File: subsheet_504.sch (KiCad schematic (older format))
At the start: 36 parts, among them J502 Phono LEFT, J503 Phono RIGHT, U504 LF347N_mu, U508 LMC1992CCN_PHY

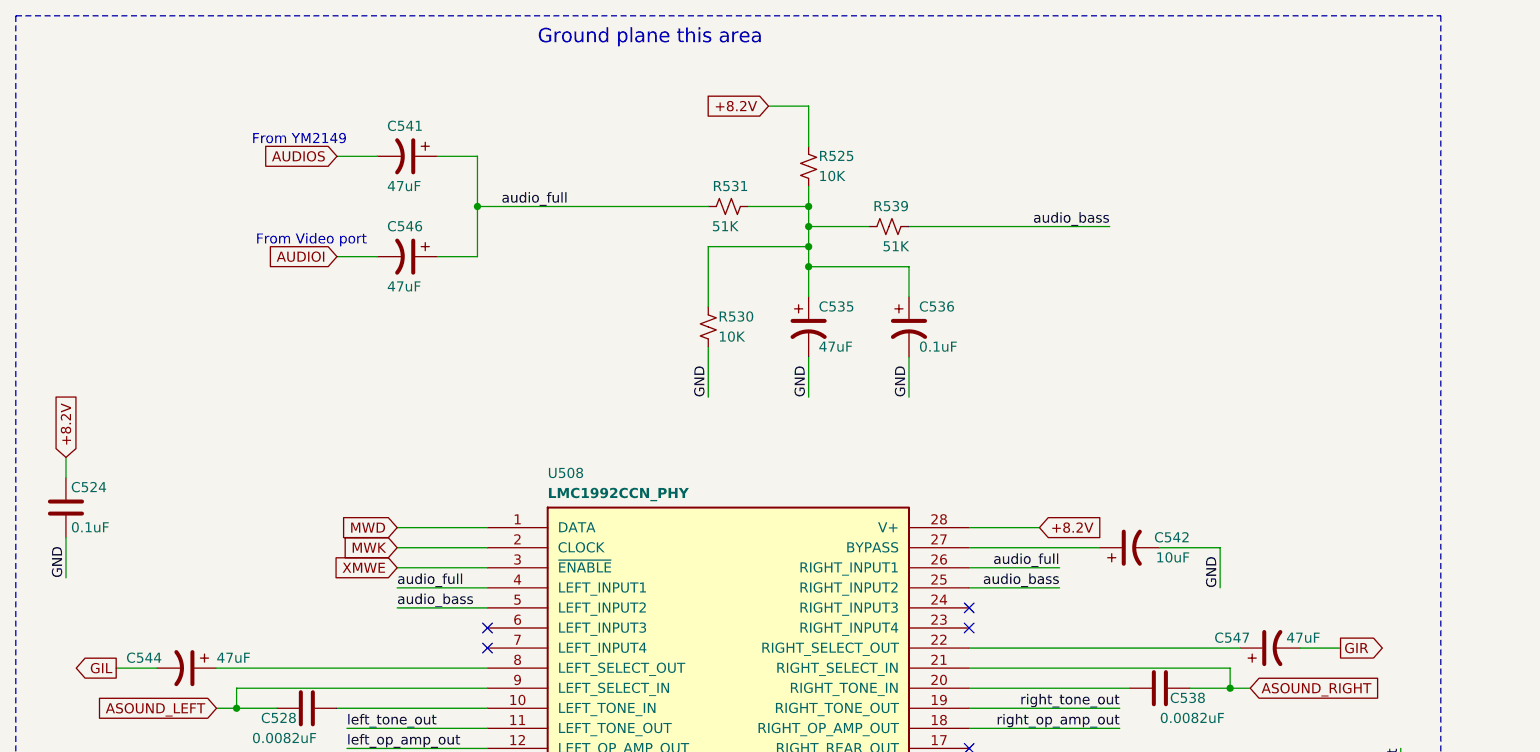
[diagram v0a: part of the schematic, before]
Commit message: [Schematic] mention and reference of the LMC Mixer fix
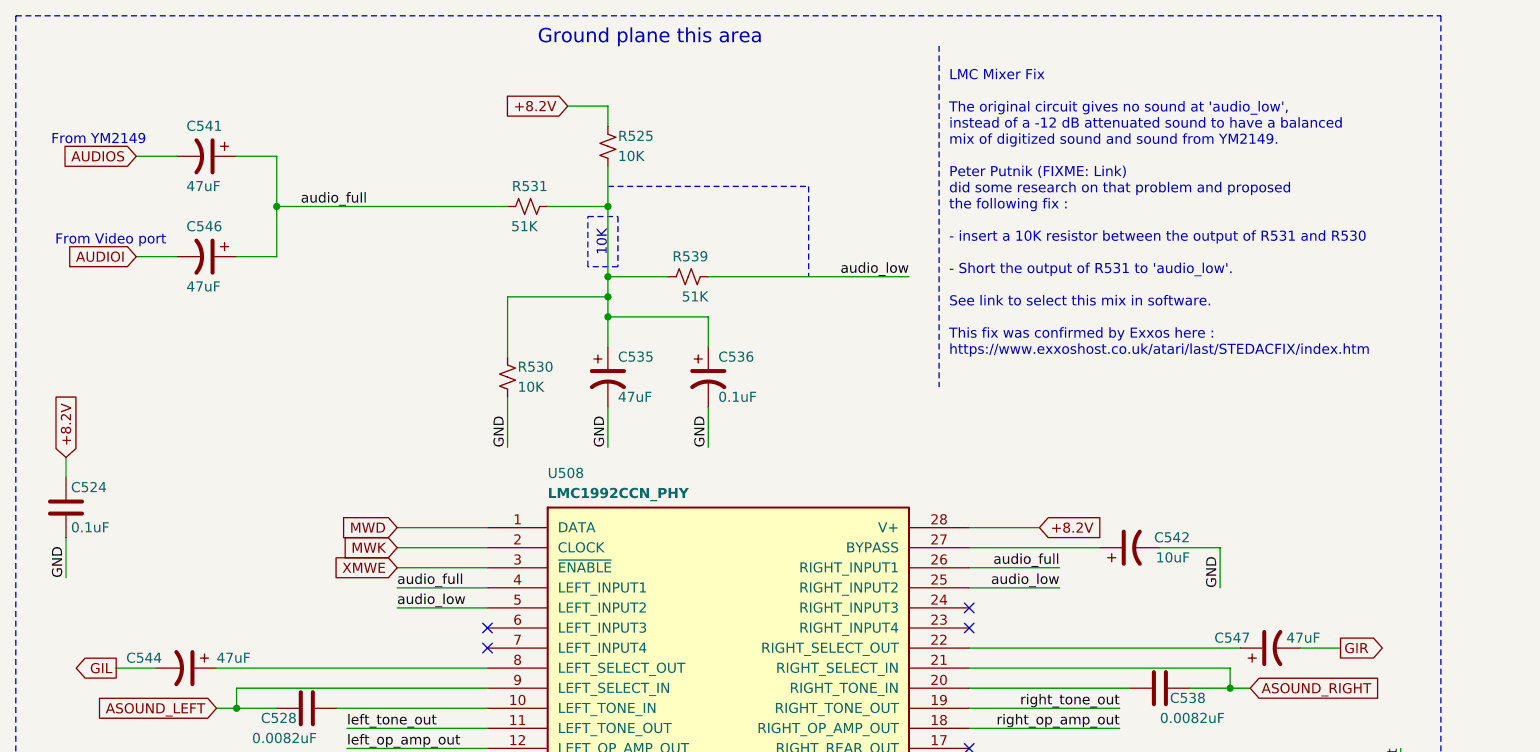
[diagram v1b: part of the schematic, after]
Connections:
- net audio_bass renamed audio_low
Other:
- note added: "10K"
- note added: "LMC Mixer Fix\n\nThe original circuit gives no sound at 'audio_low',\ninstead of a -12 dB attenuated sound to have a balanced\nmix of digitized sound and sound from YM2149.\n\nPeter Putnik (FIXME: Link) \ndid some research on that problem and proposed \nthe following fix :\n\n- insert a 10K resistor between the output of R531 and R530\n\n- Short the output of R531 to 'audio_low'. \n\nSee link to 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"
- moved on the sheet: C535, C536, C541, C546, R525, R530, R531, R539

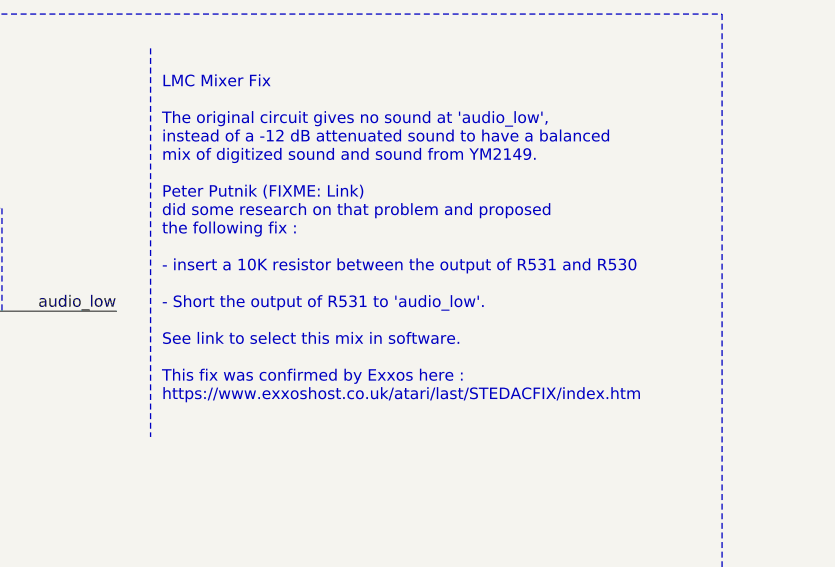
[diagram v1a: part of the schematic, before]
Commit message: [Schematics] finalize comment about audio mix fix with reference link to P.P. page
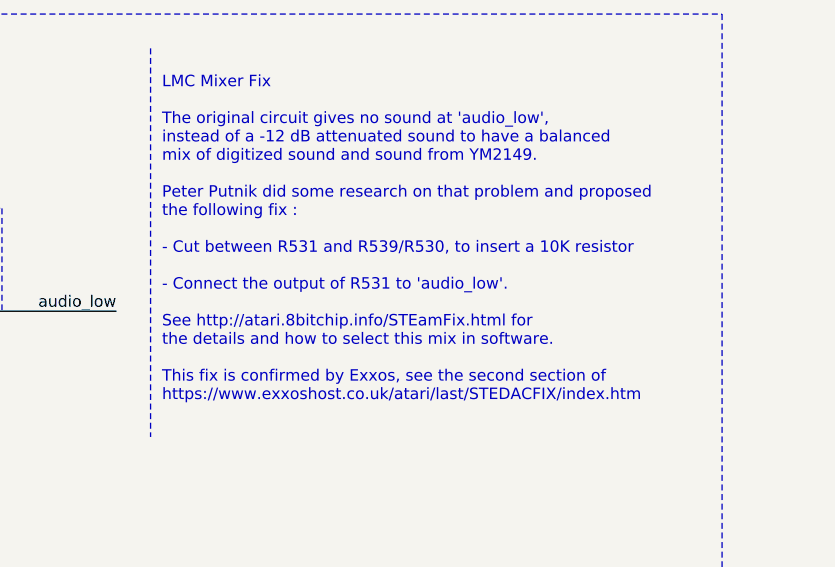
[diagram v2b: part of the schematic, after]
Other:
- note added: "LMC Mixer Fix\n\nThe original circuit gives no sound at 'audio_low',\ninstead of a -12 dB attenuated sound to have a balanced\nmix of digitized sound and sound from YM2149.\n\nPeter Putnik did some research on that problem and proposed \nthe following fix :\n\n- Cut between R531 and R539/R530, to insert a 10K resistor\n \n- Connect the output of R531 to 'audio_low'. \n\nSee http://atari.8bitchip.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"
- note removed: "LMC Mixer Fix\n\nThe original circuit gives no sound at 'audio_low',\ninstead of a -12 dB attenuated sound to have a balanced\nmix of digitized sound and sound from YM2149.\n\nPeter Putnik (FIXME: Link) \ndid some research on that problem and proposed \nthe following fix :\n\n- insert a 10K resistor between the output of R531 and R530\n\n- Short the output of R531 to 'audio_low'. \n\nSee link to 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"
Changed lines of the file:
@@
 	7450 4200 7450 4850
 Text Notes 5200 2250 0    50   ~ 0
-LMC Mixer Fix\n\nThe original circuit gives no sound at 'audio_low',\ninstead of a -12 dB attenuated sound to have a balanced\nmix of digitized sound and sound from YM2149.\n\nPeter Putnik (FIXME: Link) \ndid some research on that problem and proposed \nthe following fix :\n\n- insert a 10K resistor between the output of R531 and R530\n\n- Short the output of R531 to 'audio_low'. \n\nSee link to select this mix in software.\n\nThis fix was confirmed by Exxos here :\nhttps://www.exxoshost.co.uk/atari/last/STEDACFIX/index.htm
+LMC Mixer Fix\n\nThe original circuit gives no sound at 'audio_low',\ninstead of a -12 dB attenuated sound to have a balanced\nmix of digitized sound and sound from YM2149.\n\nPeter Putnik did some research on that problem and proposed \nthe following fix :\n\n- Cut between R531 and R539/R530, to insert a 10K resistor\n  \n- Connect the output of R531 to 'audio_low'. \n\nSee http://atari.8bitchip.info/STEamFix.html for \nthe details and how to select this mix in software.\n\nThis fix is confirmed by Exxos, see the second section of\nhttps://www.exxoshost.co.uk/atari/last/STEDACFIX/index.htm\n
 Connection ~ 3500 1950
 Text Notes 3500 1750 1    50   ~ 0

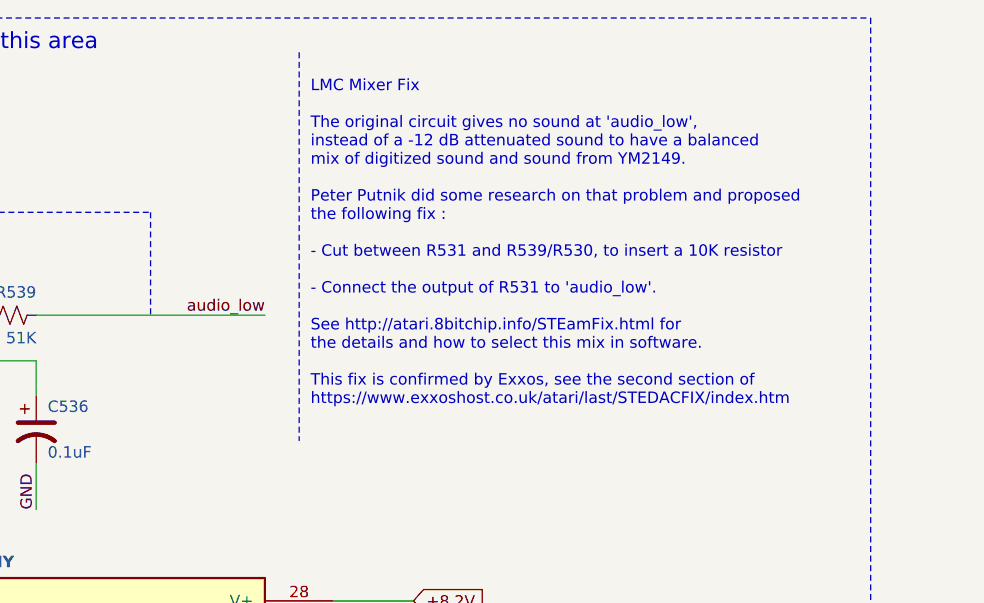
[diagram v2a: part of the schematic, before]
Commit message: Added a note about the presence of comment referencing some hardware fixes
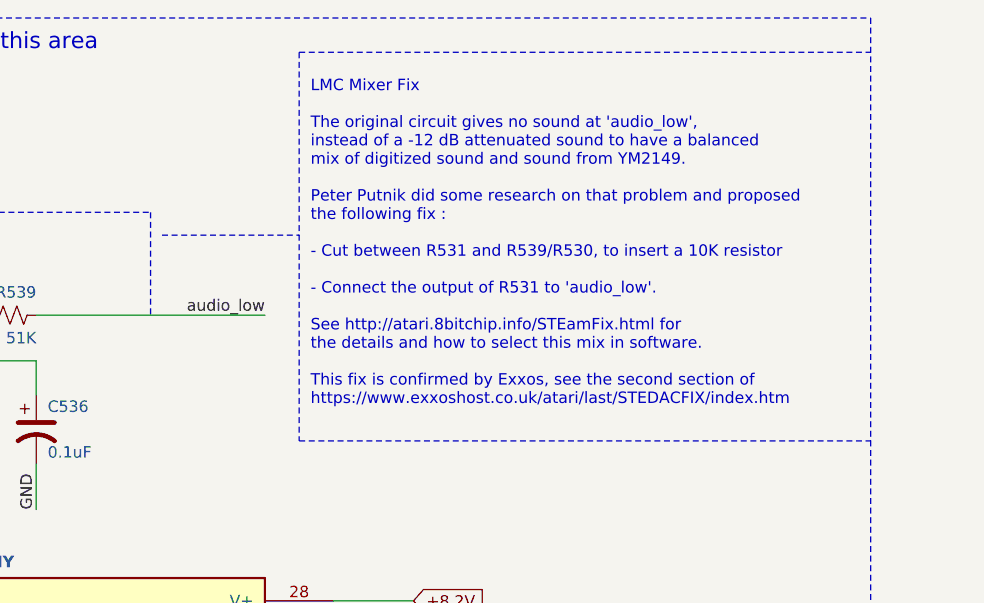
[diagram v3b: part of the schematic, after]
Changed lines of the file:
@@
 Wire Notes Line
 	5150 700  5150 2400
+Wire Notes Line
+	4550 1500 5150 1500
+Wire Notes Line
+	5150 700  7650 700
+Wire Notes Line
+	5150 2400 7650 2400
 $EndSCHEMATC
